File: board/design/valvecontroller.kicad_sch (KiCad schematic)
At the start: 13 parts, among them J1 Jack-DC, J2 Jack-DC, J3 Screw_Terminal_01x02, J4 Valve+, J5 Valve-, K1 G5V-1

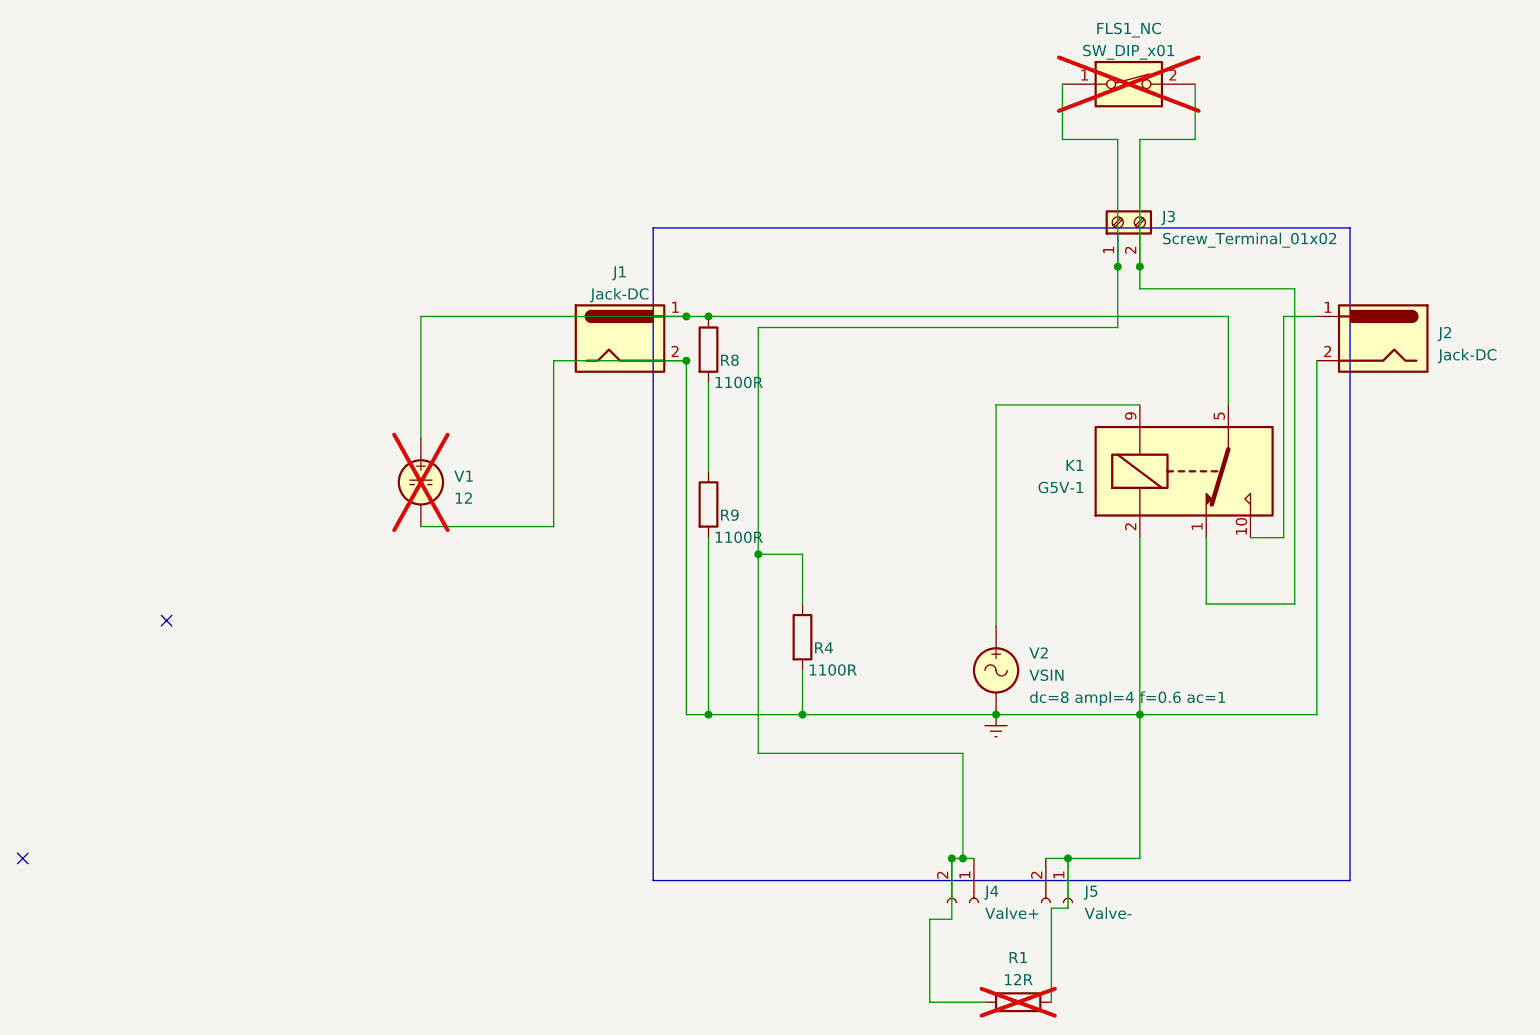
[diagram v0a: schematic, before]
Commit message: use ne555d
this will not be able to reset. We need actually an opposite device or invert nearly every input
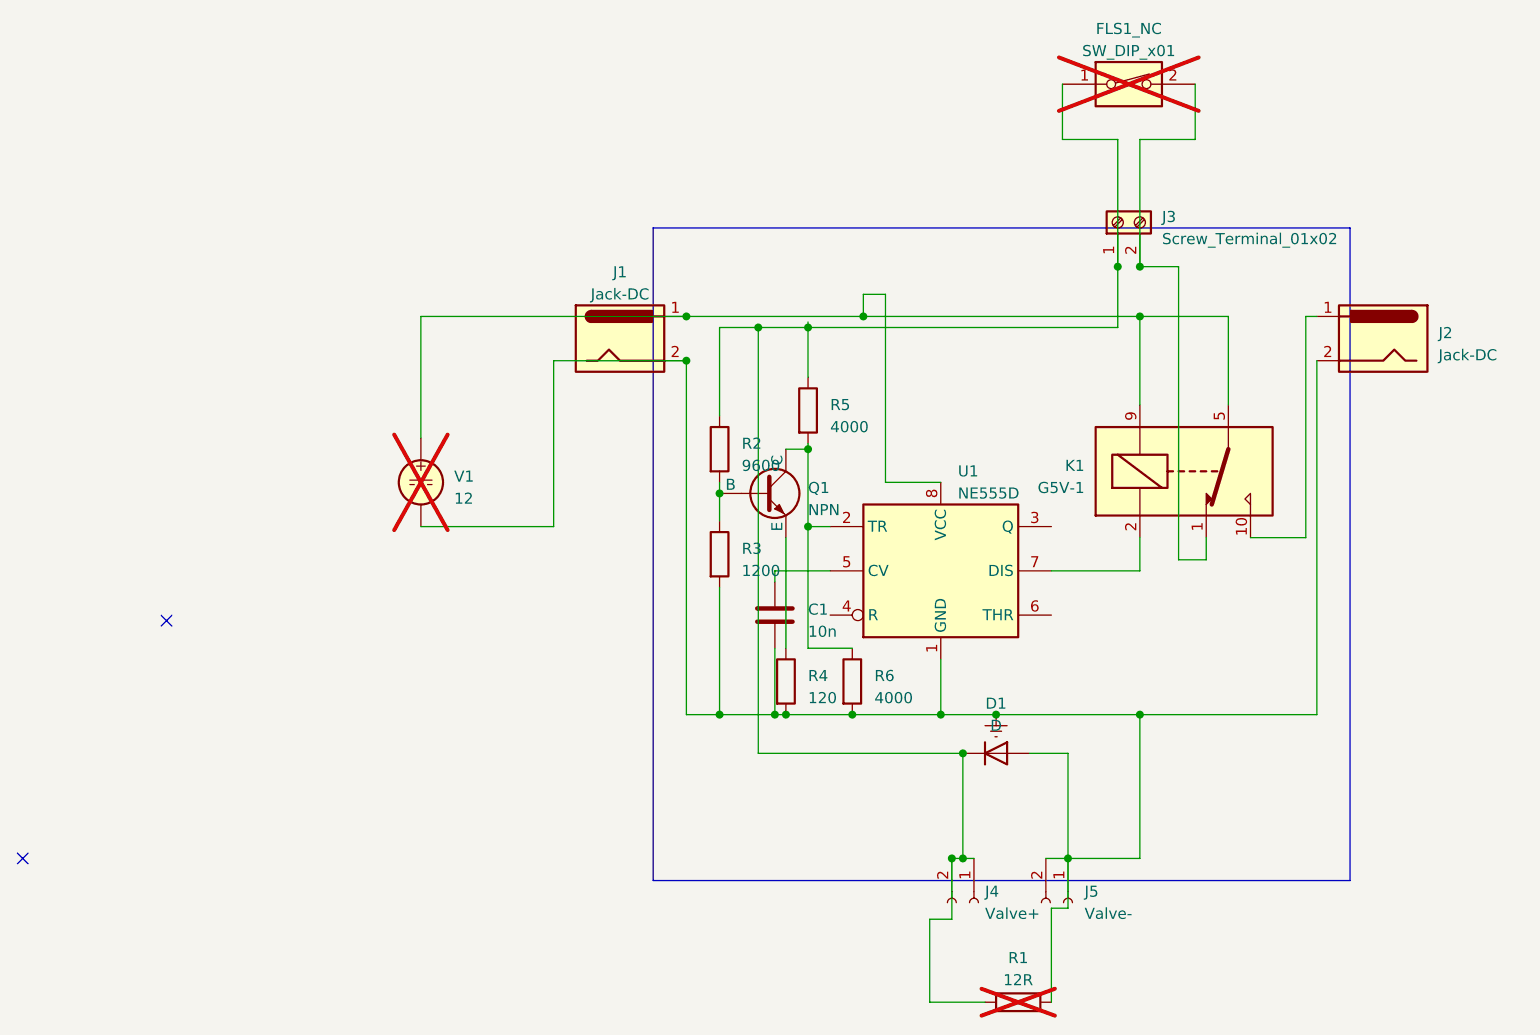
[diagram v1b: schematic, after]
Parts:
- removed R8, R9: 1100R, symbol Device:R
- removed V2: VSIN, symbol Simulation_SPICE:VSIN
- added C1: 10n, symbol Device:C
- added D1: D, symbol Device:D
- added Q1: NPN, symbol Simulation_SPICE:NPN
- added R2: 9600, symbol Device:R
- added R3: 1200, symbol Device:R
- added R5, R6: 4000, symbol Device:R
- added U1: NE555D, Package_SO:SOIC-8_3.9x4.9mm_P1.27mm, symbol Timer:NE555D
- R4: value 1100R -> 120
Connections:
- net Earth: now also C1.2, D1.2 (A), R3.2, R6.2, U1.1 (GND); no longer K1.2
- net at FLS1_NC.1, J3.1 (Pin_1), J4.1 (Pin_1)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: now also D1.1 (K), R2.1, R5.1; no longer R4.1
- net at J1.1, K1.5, K1.6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: now also K1.9, U1.8 (VCC)
- new net: Q1.3 (E), R4.1
- new net: K1.2, U1.7 (DIS)
- new net: Q1.1 (C), R5.2, R6.1, U1.2 (TR)
- new net: Q1.2 (B), R2.2, R3.1
- new net: C1.1, U1.5 (CV)

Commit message: proposal1 for ne555 version
the valve is no more switched directly, but while the relay is on
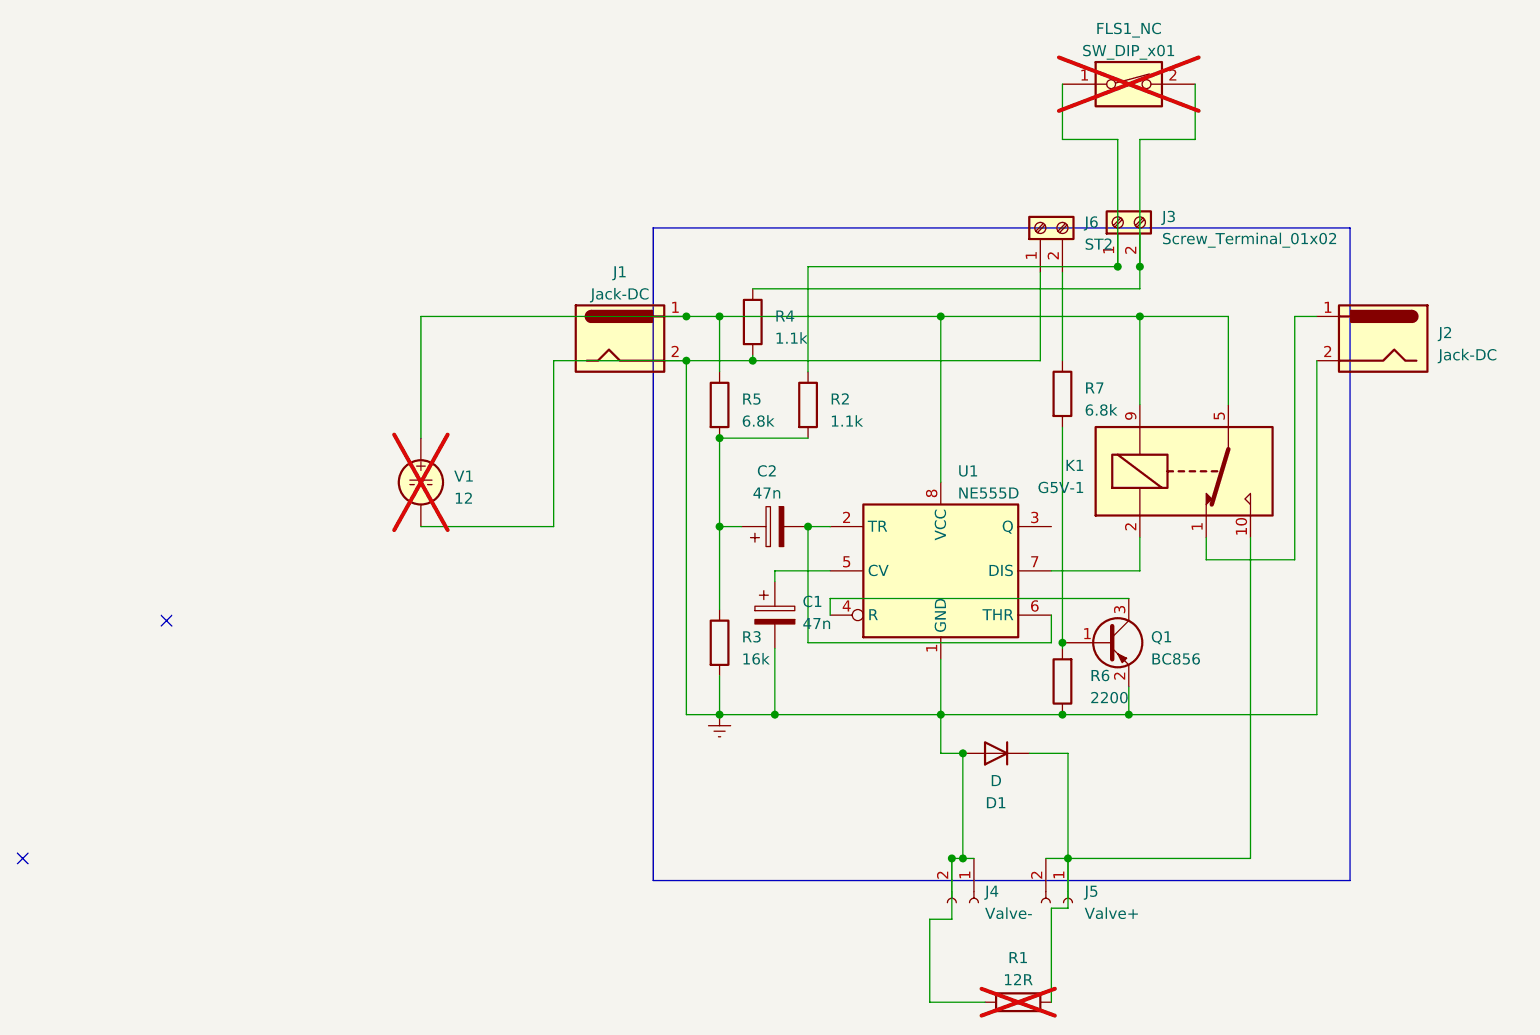
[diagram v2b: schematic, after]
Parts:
- removed C1: 10n, symbol Device:C
- removed Q1: NPN, symbol Simulation_SPICE:NPN
- added C1, C2: 47n, symbol Device:C_Polarized
- added J6: ST2, symbol Connector:Screw_Terminal_01x02
- added Q1: BC856, Package_TO_SOT_SMD:SOT-23, symbol Transistor_BJT:BC856
- added R7: 6.8k, symbol Device:R
- J4: value Valve+ -> Valve-
- J5: value Valve- -> Valve+
- R2: value 9600 -> 1.1k
- R3: value 1200 -> 16k
- R4: value 120 -> 1.1k
- R5: value 4000 -> 6.8k
- R6: value 4000 -> 2200
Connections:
- net Earth: now also J4.1 (Pin_1), J4.2 (Pin_2), R1.1, R6.1, C1.2, J6.1 (Pin_1), Q1.2 (E); no longer J5.1 (Pin_1), J5.2 (Pin_2), R1.2, R6.2
- net at R4.1: now also FLS1_NC.2, J3.2 (Pin_2)
- net at K1.10: now also D1.1 (K), J5.1 (Pin_1), J5.2 (Pin_2), R1.2; no longer J2.1
- net at J1.1, K1.5, K1.6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: now also R5.1
- net at R2.2, R3.1: now also R5.2, C2.1
- net at U1.5 (CV): now also C1.1
- net at U1.4 (R): now also Q1.3 (C)
- net at U1.6 (THR): now also U1.2 (TR), C2.2
- new net: J2.1, K1.1
- new net: Q1.1 (B), R6.2, R7.2
- new net: FLS1_NC.1, J3.1 (Pin_1), R2.1
- new net: J6.2 (Pin_2), R7.1
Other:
- moved on the sheet: D1, R3
